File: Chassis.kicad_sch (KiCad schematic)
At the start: 15 parts, among them J1 Conn_01x02, J10 Conn_01x02, J2 Conn_01x02, J3 Conn_01x02, J4 Conn_01x02, J5 Conn_01x02, J6 Conn_01x02, J7 Conn_01x02, J8 Conn_01x02, J9 Conn_01x02

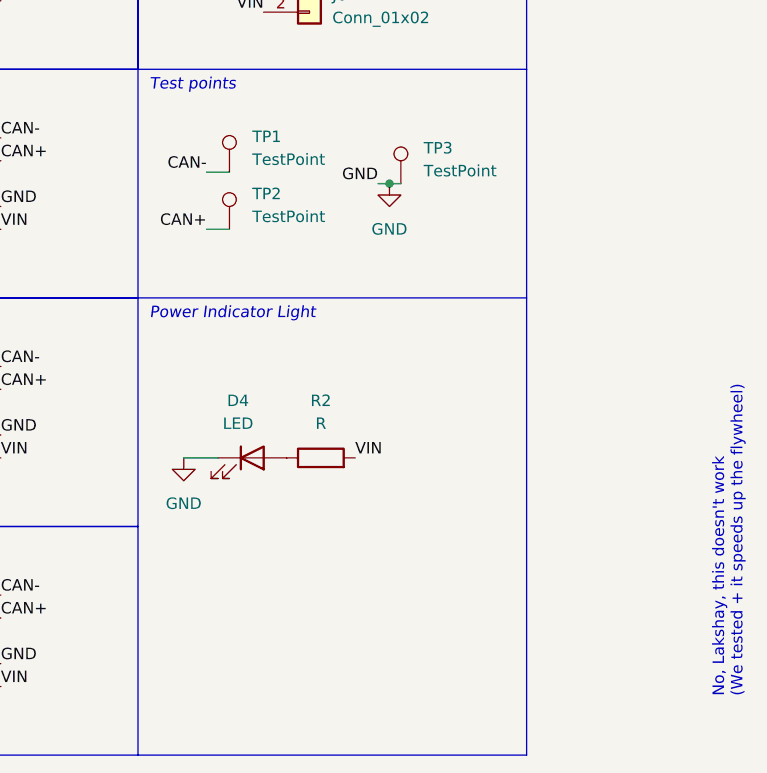
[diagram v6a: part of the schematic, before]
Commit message: Edit test point placement
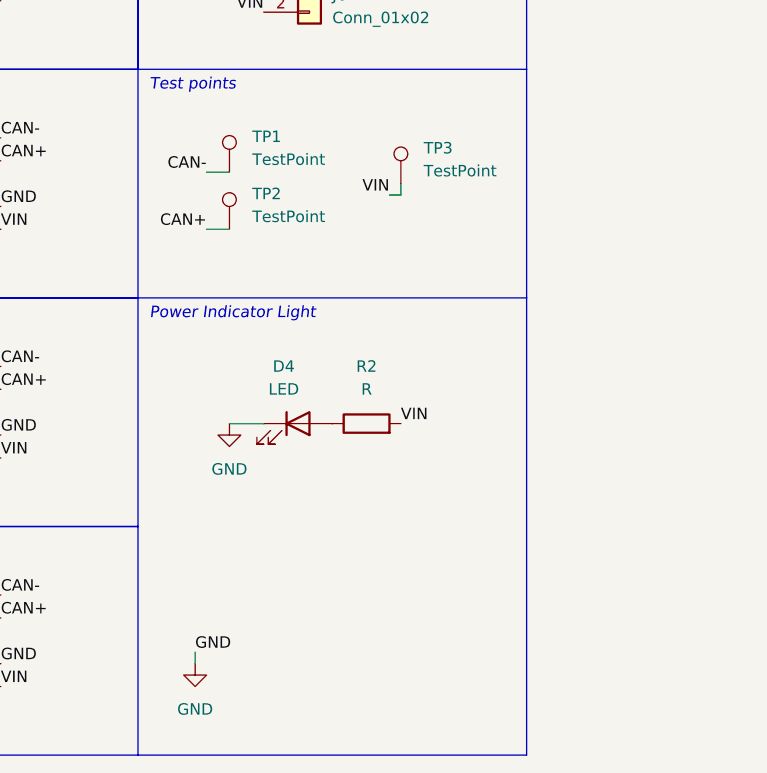
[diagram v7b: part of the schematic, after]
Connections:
- net GND: no longer TP3.1
- net VIN: now also TP3.1
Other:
- note removed: "No, Lakshay, this doesn't work (We tested + it speeds up the flywheel)"
- moved on the sheet: D4, R2
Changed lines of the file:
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@@
 (kicad_sch (version 20230121) (generator eeschema)
   (paper "A4")
-  (junction (at 176.53 95.25) (diameter 0) (color 0 0 0 0)
-  )
   (polyline (pts (xy 191.77 82.55) (xy 191.77 107.95))
     (stroke (width 0) (type default))
@@
     (stroke (width 0) (type default))
   )
-  (wire (pts (xy 176.53 95.25) (xy 177.8 95.25))
+  (wire (pts (xy 177.8 96.52) (xy 177.8 95.25))
     (stroke (width 0) (type default))
   )
@@
     (stroke (width 0) (type default))
   )
+  (wire (pts (xy 176.53 96.52) (xy 177.8 96.52))
+    (stroke (width 0) (type default))
+  )
   (polyline (pts (xy 148.59 158.75) (xy 191.77 158.75))
     (stroke (width 0) (type default))
   )
-  (wire (pts (xy 175.26 95.25) (xy 176.53 95.25))
-    (stroke (width 0) (type default))
-  )
-  (wire (pts (xy 153.67 125.73) (xy 157.48 125.73))
+  (wire (pts (xy 158.75 121.92) (xy 162.56 121.92))
     (stroke (width 0) (type default))
   )
@@
     (stroke (width 0) (type default))
   )
+  (wire (pts (xy 154.94 147.32) (xy 154.94 148.59))
+    (stroke (width 0) (type default))
+  )
   (rectangle (start 105.41 107.95) (end 148.59 133.35)
     (stroke (width 0) (type default))
@@
     (fill (type none))
   )
-  (text "No, Lakshay, this doesn't work\n(We tested + it speeds up the flywheel)"
-    (at 215.9 152.4 90)
-    (effects (font (size 1.27 1.27)) (justify left bottom))
-  )
   (text "to BR ESC\n" (at 106.68 85.09 0)
     (effects (font (size 1.27 1.27) italic) (justify left bottom))
@@
     (effects (font (size 1.27 1.27)) (justify left bottom))
   )
-  (label "GND" (at 175.26 95.25 180) (fields_autoplaced)
-    (effects (font (size 1.27 1.27)) (justify right bottom))
-  )
   (label "CAN-" (at 133.35 90.17 0) (fields_autoplaced)
     (effects (font (size 1.27 1.27)) (justify left bottom))
@@
     (effects (font (size 1.27 1.27)) (justify left bottom))
   )
-  (label "VIN" (at 172.72 125.73 0) (fields_autoplaced)
+  (label "VIN" (at 177.8 121.92 0) (fields_autoplaced)
     (effects (font (size 1.27 1.27)) (justify left bottom))
   )
@@
     (effects (font (size 1.27 1.27)) (justify left bottom))
   )
+  (label "VIN" (at 176.53 96.52 180) (fields_autoplaced)
+    (effects (font (size 1.27 1.27)) (justify right bottom))
+  )
   (label "VIN" (at 133.35 125.73 0) (fields_autoplaced)
     (effects (font (size 1.27 1.27)) (justify left bottom))
@@
     (effects (font (size 1.27 1.27)) (justify right bottom))
   )
+  (label "GND" (at 154.94 147.32 0) (fields_autoplaced)
+    (effects (font (size 1.27 1.27)) (justify left bottom))
+  )
   (label "GND" (at 133.35 97.79 0) (fields_autoplaced)
     (effects (font (size 1.27 1.27)) (justify left bottom))
@@
     )
   )
-  (symbol (lib_id "power:GND") (at 153.67 125.73 0) (unit 1)
-    (in_bom yes) (on_board yes) (dnp no) (fields_autoplaced)
-    (property "Reference" "#PWR01" (at 153.67 132.08 0)
-      (effects (font (size 1.27 1.27)) hide)
-    )
-    (property "Value" "GND" (at 153.67 130.81 0)
-      (effects (font (size 1.27 1.27)))
-    )
-    (property "Footprint" "" (at 153.67 125.73 0)
-      (effects (font (size 1.27 1.27)) hide)
-    )
-    (property "Datasheet" "" (at 153.67 125.73 0)
+  (symbol (lib_id "power:GND") (at 158.75 121.92 0) (unit 1)
+    (in_bom yes) (on_board yes) (dnp no) (fields_autoplaced)
+    (property "Reference" "#PWR01" (at 158.75 128.27 0)
+      (effects (font (size 1.27 1.27)) hide)
+    )
+    (property "Value" "GND" (at 158.75 127 0)
+      (effects (font (size 1.27 1.27)))
+    )
+    (property "Footprint" "" (at 158.75 121.92 0)
+      (effects (font (size 1.27 1.27)) hide)
+    )
+    (property "Datasheet" "" (at 158.75 121.92 0)
       (effects (font (size 1.27 1.27)) hide)
     )
@@
     )
   )
+  (symbol (lib_id "power:GND") (at 154.94 148.59 0) (unit 1)
+    (in_bom yes) (on_board yes) (dnp no) (fields_autoplaced)
+    (property "Reference" "#PWR02" (at 154.94 154.94 0)
+      (effects (font (size 1.27 1.27)) hide)
+    )
+    (property "Value" "GND" (at 154.94 153.67 0)
+      (effects (font (size 1.27 1.27)))
+    )
+    (property "Footprint" "" (at 154.94 148.59 0)
+      (effects (font (size 1.27 1.27)) hide)
+    )
+    (property "Datasheet" "" (at 154.94 148.59 0)
+      (effects (font (size 1.27 1.27)) hide)
+    )
+    (pin "1")
+    (instances
+      (project "Chassis"
+        (path "/d5f28ba3-2393-441a-9a3a-5aa9d797472a"
+          (reference "#PWR02") (unit 1)
+        )
+      )
+    )
+  )
   (symbol (lib_id "Connector_Generic:Conn_01x02") (at 128.27 97.79 0) (mirror y) (unit 1)
     (in_bom yes) (on_board yes) (dnp no) (fields_autoplaced)
@@
     )
   )
-  (symbol (lib_id "Device:LED") (at 161.29 125.73 0) (unit 1)
-    (in_bom yes) (on_board yes) (dnp no) (fields_autoplaced)
-    (property "Reference" "D4" (at 159.7025 119.38 0)
-      (effects (font (size 1.27 1.27)))
-    )
-    (property "Value" "LED" (at 159.7025 121.92 0)
-      (effects (font (size 1.27 1.27)))
-    )
-    (property "Footprint" "LED_SMD:LED_0603_1608Metric_Pad1.05x0.95mm_HandSolder" (at 161.29 125.73 0)
-      (effects (font (size 1.27 1.27)) hide)
-    )
-    (property "Datasheet" "~" (at 161.29 125.73 0)
+  (symbol (lib_id "Device:LED") (at 166.37 121.92 0) (unit 1)
+    (in_bom yes) (on_board yes) (dnp no) (fields_autoplaced)
+    (property "Reference" "D4" (at 164.7825 115.57 0)
+      (effects (font (size 1.27 1.27)))
+    )
+    (property "Value" "LED" (at 164.7825 118.11 0)
+      (effects (font (size 1.27 1.27)))
+    )
+    (property "Footprint" "LED_SMD:LED_0603_1608Metric_Pad1.05x0.95mm_HandSolder" (at 166.37 121.92 0)
+      (effects (font (size 1.27 1.27)) hide)
+    )
+    (property "Datasheet" "~" (at 166.37 121.92 0)
       (effects (font (size 1.27 1.27)) hide)
     )
@@
     )
   )
-  (symbol (lib_id "power:GND") (at 176.53 95.25 0) (unit 1)
-    (in_bom yes) (on_board yes) (dnp no) (fields_autoplaced)
-    (property "Reference" "#PWR02" (at 176.53 101.6 0)
-      (effects (font (size 1.27 1.27)) hide)
-    )
-    (property "Value" "GND" (at 176.53 100.33 0)
-      (effects (font (size 1.27 1.27)))
-    )
-    (property "Footprint" "" (at 176.53 95.25 0)
-      (effects (font (size 1.27 1.27)) hide)
-    )
-    (property "Datasheet" "" (at 176.53 95.25 0)
-      (effects (font (size 1.27 1.27)) hide)
-    )
-    (pin "1")
-    (instances
-      (project "Chassis"
-        (path "/d5f28ba3-2393-441a-9a3a-5aa9d797472a"
-          (reference "#PWR02") (unit 1)
-        )
-      )
-    )
-  )
   (symbol (lib_id "Connector_Generic:Conn_01x02") (at 128.27 123.19 0) (mirror y) (unit 1)
     (in_bom yes) (on_board yes) (dnp no) (fields_autoplaced)
@@
     )
   )
-  (symbol (lib_id "Device:R") (at 168.91 125.73 90) (unit 1)
-    (in_bom yes) (on_board yes) (dnp no) (fields_autoplaced)
-    (property "Reference" "R2" (at 168.91 119.38 90)
-      (effects (font (size 1.27 1.27)))
-    )
-    (property "Value" "R" (at 168.91 121.92 90)
-      (effects (font (size 1.27 1.27)))
-    )
-    (property "Footprint" "Resistor_SMD:R_0603_1608Metric_Pad0.98x0.95mm_HandSolder" (at 168.91 127.508 90)
-      (effects (font (size 1.27 1.27)) hide)
-    )
-    (property "Datasheet" "~" (at 168.91 125.73 0)
-      (effects (font (size 1.27 1.27)) hide)
-    )
+  (symbol (lib_id "Device:R") (at 173.99 121.92 90) (unit 1)
+    (in_bom yes) (on_board yes) (dnp no) (fields_autoplaced)
+    (property "Reference" "R2" (at 173.99 115.57 90)
+      (effects (font (size 1.27 1.27)))
+    )
+    (property "Value" "R" (at 173.99 118.11 90)
+      (effects (font (size 1.27 1.27)))
+    )
+    (property "Footprint" "Resistor_SMD:R_0603_1608Metric_Pad0.98x0.95mm_HandSolder" (at 173.99 123.698 90)
+      (effects (font (size 1.27 1.27)) hide)
+    )
+    (property "Datasheet" "~" (at 173.99 121.92 0)
+      (effects (font (size 1.27 1.27)) hide)
+    )

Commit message: Completed initial layout
I'm going to get roasted over some of these choices
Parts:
- removed TP3: TestPoint, TestPoint:TestPoint_Pad_1.0x1.0mm, symbol Connector:TestPoint
- added D3: 150060BS75000, LED_SMD:LED_0603_1608Metric_Pad1.05x0.95mm_HandSolder, symbol Device:LED
- added R6: 680Ω, Resistor_SMD:R_0603_1608Metric_Pad0.98x0.95mm_HandSolder, symbol Device:R
- D4: value LED -> 150060RS75000
- R2: value R -> 1kΩ
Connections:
- net GND: now also D3.1 (K)
- net VIN renamed +24V
- new net: D3.2 (A), R6.2
- new net V_{OUT}: R6.1
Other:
- added sheet 24V -> 19V Buck Convertor (buck.kicad_sch)
- note added: "+ indicator LED"
- note added: "Buck Convertor"
- note added: "Test points & Indicator light"
- note removed: "Power Indicator Light"
- note removed: "Test points"
- moved on the sheet: D4, J5, J6, R2
